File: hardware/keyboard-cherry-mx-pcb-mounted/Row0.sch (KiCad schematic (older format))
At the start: 28 parts, among them SW1 ESC, SW10 F12, SW11 F5, SW12 Delete, SW13 F6, SW14 F7, SW2 F8, SW3 F1, SW4 F9, SW5 F2, SW6 F10, SW7 F2, SW8 F11, SW9 F4

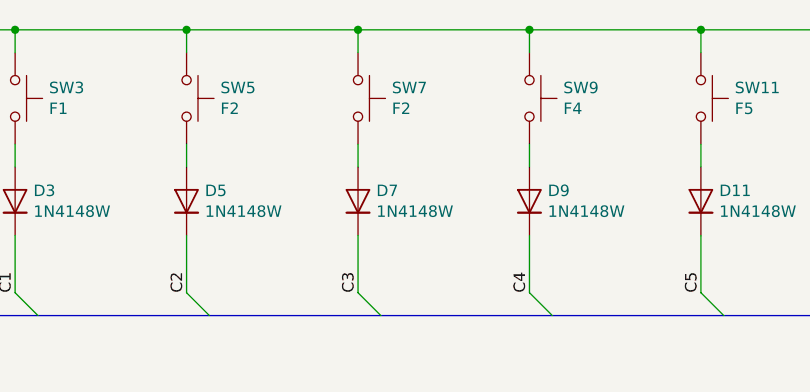
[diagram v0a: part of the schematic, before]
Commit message: Adds general layout for the custom keyboard.
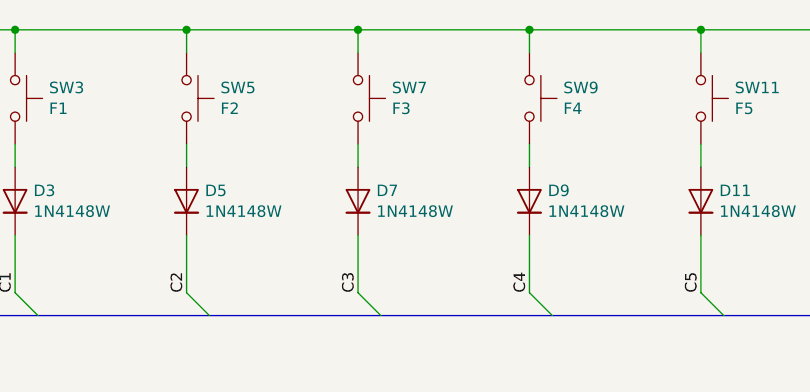
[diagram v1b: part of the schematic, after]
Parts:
- SW7: value F2 -> F3
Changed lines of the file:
@@
 AR Path="/5E697948/5E6CDE4B/5E6D9975" Ref="SW7"  Part="1"
 F 0 "SW7" V 5304 2848 50  0000 L CNN
-F 1 "F2" V 5395 2848 50  0000 L CNN
+F 1 "F3" V 5395 2848 50  0000 L CNN
 F 2 "Button_Switch_Keyboard:SW_Cherry_MX_1.00u_PCB" H 5350 2900 50  0001 C CNN
 F 3 "~" H 5350 2900 50  0001 C CNN
@@
 Text Label 2800 3650 2    50   ~ 0
 C[0..15]
+Connection ~ 6850 4500
+Wire Wire Line
+	6850 4500 9350 4500
+Wire Wire Line
+	9350 2400 9350 4500
+Connection ~ 8350 2400
+Wire Wire Line
+	8350 2400 9350 2400
 Wire Bus Line
 	2800 5750 6950 5750
 Wire Bus Line
 	2800 3650 8450 3650
-Connection ~ 6850 4500
-Wire Wire Line
-	6850 4500 9350 4500
-Wire Wire Line
-	9350 2400 9350 4500
-Connection ~ 8350 2400
-Wire Wire Line
-	8350 2400 9350 2400
 $EndSCHEMATC

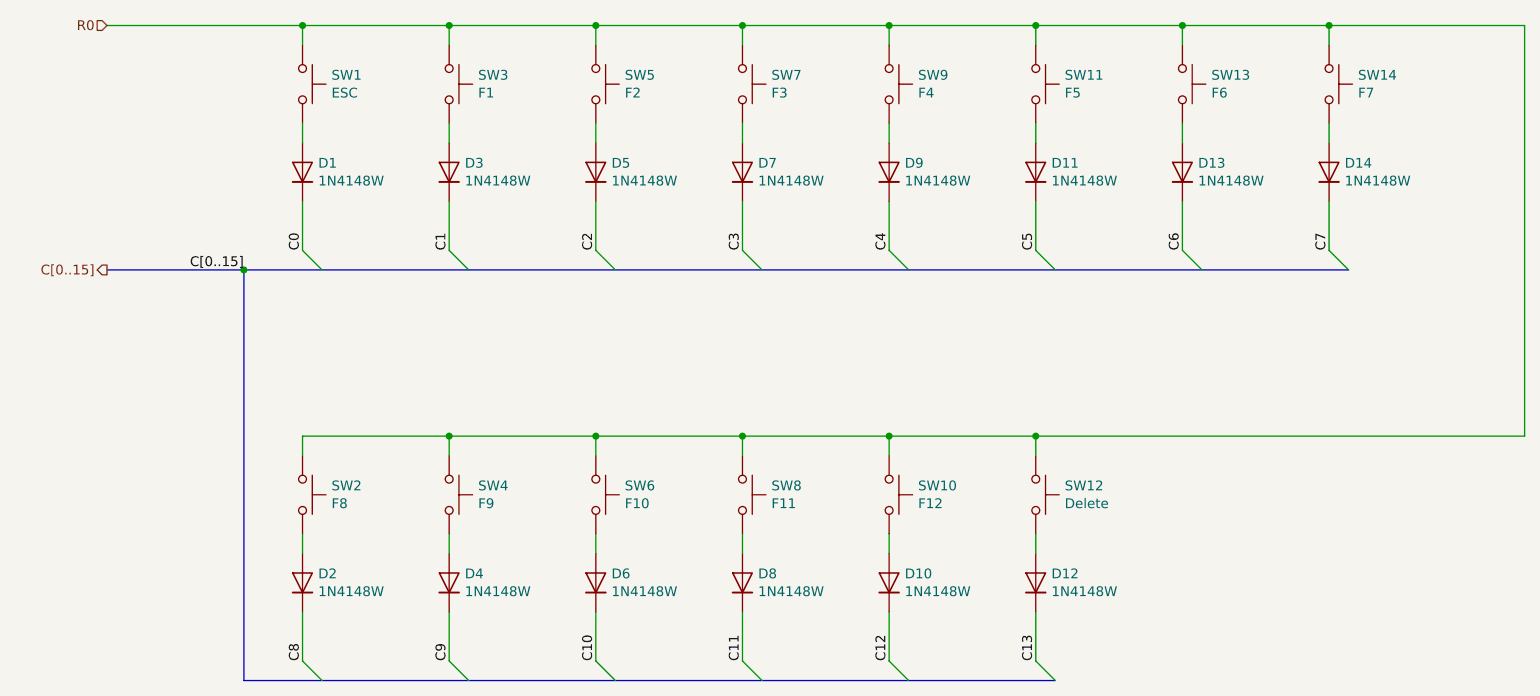
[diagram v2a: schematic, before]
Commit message: Adds completed sensor and power connections. Still need to add USB footprint then sch are done for version 1.0
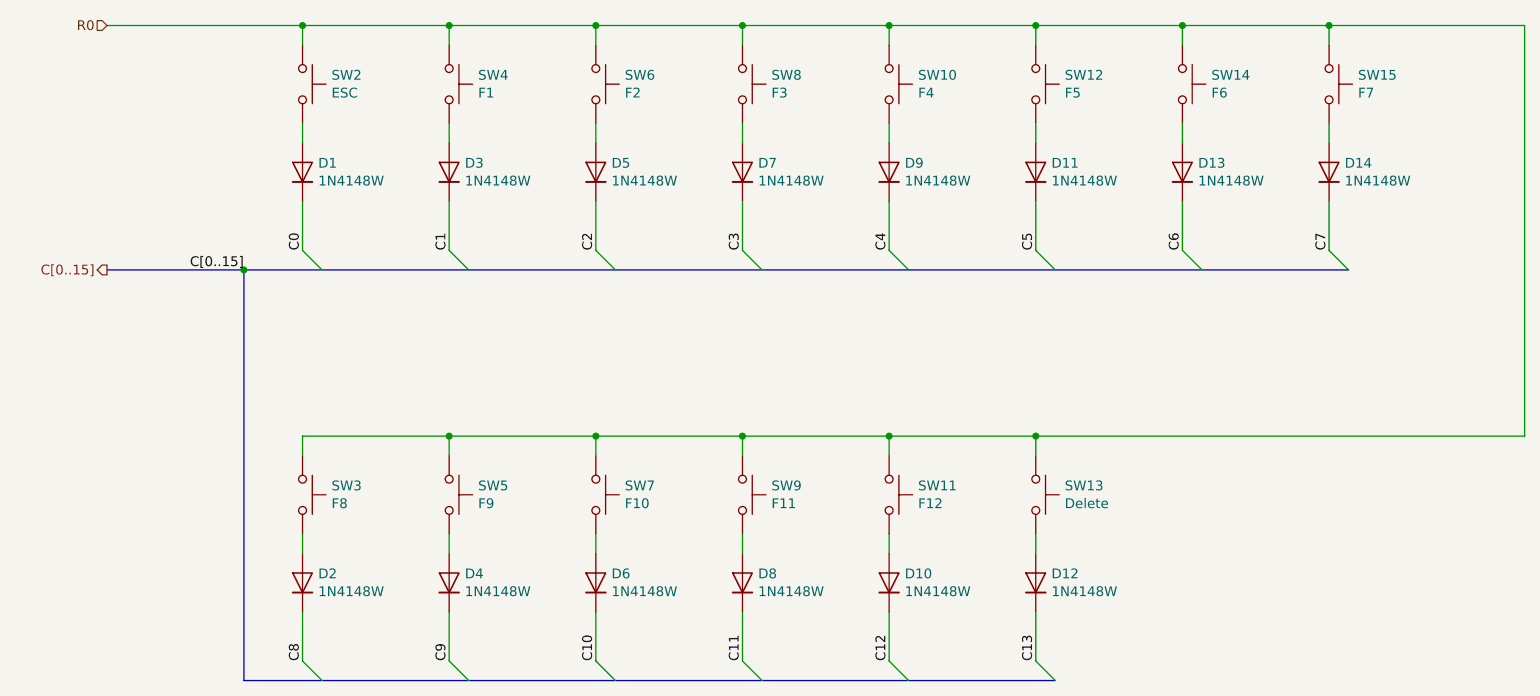
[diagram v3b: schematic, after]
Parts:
- renumbered SW9 to SW10, SW10 to SW11, SW11 to SW12, SW12 to SW13, SW13 to SW14, SW14 to SW15, SW1 to SW2, SW2 to SW3, SW3 to SW4, SW4 to SW5, SW5 to SW6, SW6 to SW7, SW7 to SW8, SW8 to SW9
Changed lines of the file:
@@
 P 3100 2700
 AR Path="/5E697948/5E6D9949" Ref="SW?"  Part="1"
-AR Path="/5E697948/5E6CDE4B/5E6D9949" Ref="SW1"  Part="1"
-F 0 "SW1" V 3054 2848 50  0000 L CNN
+AR Path="/5E697948/5E6CDE4B/5E6D9949" Ref="SW2"  Part="1"
+F 0 "SW2" V 3054 2848 50  0000 L CNN
 F 1 "ESC" V 3145 2848 50  0000 L CNN
 F 2 "Button_Switch_Keyboard:SW_Cherry_MX_1.00u_PCB" H 3100 2900 50  0001 C CNN
@@
 P 3850 2700
 AR Path="/5E697948/5E6D9959" Ref="SW?"  Part="1"
-AR Path="/5E697948/5E6CDE4B/5E6D9959" Ref="SW3"  Part="1"
-F 0 "SW3" V 3804 2848 50  0000 L CNN
+AR Path="/5E697948/5E6CDE4B/5E6D9959" Ref="SW4"  Part="1"
+F 0 "SW4" V 3804 2848 50  0000 L CNN
 F 1 "F1" V 3895 2848 50  0000 L CNN
 F 2 "Button_Switch_Keyboard:SW_Cherry_MX_1.00u_PCB" H 3850 2900 50  0001 C CNN
@@
 P 4600 2700
 AR Path="/5E697948/5E6D9967" Ref="SW?"  Part="1"
-AR Path="/5E697948/5E6CDE4B/5E6D9967" Ref="SW5"  Part="1"
-F 0 "SW5" V 4554 2848 50  0000 L CNN
+AR Path="/5E697948/5E6CDE4B/5E6D9967" Ref="SW6"  Part="1"
+F 0 "SW6" V 4554 2848 50  0000 L CNN
 F 1 "F2" V 4645 2848 50  0000 L CNN
 F 2 "Button_Switch_Keyboard:SW_Cherry_MX_1.00u_PCB" H 4600 2900 50  0001 C CNN
@@
 P 5350 2700
 AR Path="/5E697948/5E6D9975" Ref="SW?"  Part="1"
-AR Path="/5E697948/5E6CDE4B/5E6D9975" Ref="SW7"  Part="1"
-F 0 "SW7" V 5304 2848 50  0000 L CNN
+AR Path="/5E697948/5E6CDE4B/5E6D9975" Ref="SW8"  Part="1"
+F 0 "SW8" V 5304 2848 50  0000 L CNN
 F 1 "F3" V 5395 2848 50  0000 L CNN
 F 2 "Button_Switch_Keyboard:SW_Cherry_MX_1.00u_PCB" H 5350 2900 50  0001 C CNN
@@
 P 6100 2700
 AR Path="/5E697948/5E6D9983" Ref="SW?"  Part="1"
-AR Path="/5E697948/5E6CDE4B/5E6D9983" Ref="SW9"  Part="1"
-F 0 "SW9" V 6054 2848 50  0000 L CNN
+AR Path="/5E697948/5E6CDE4B/5E6D9983" Ref="SW10"  Part="1"
+F 0 "SW10" V 6054 2848 50  0000 L CNN
 F 1 "F4" V 6145 2848 50  0000 L CNN
 F 2 "Button_Switch_Keyboard:SW_Cherry_MX_1.00u_PCB" H 6100 2900 50  0001 C CNN
@@
 P 6850 2700
 AR Path="/5E697948/5E6D9991" Ref="SW?"  Part="1"
-AR Path="/5E697948/5E6CDE4B/5E6D9991" Ref="SW11"  Part="1"
-F 0 "SW11" V 6804 2848 50  0000 L CNN
+AR Path="/5E697948/5E6CDE4B/5E6D9991" Ref="SW12"  Part="1"
+F 0 "SW12" V 6804 2848 50  0000 L CNN
 F 1 "F5" V 6895 2848 50  0000 L CNN
 F 2 "Button_Switch_Keyboard:SW_Cherry_MX_1.00u_PCB" H 6850 2900 50  0001 C CNN
@@
 P 7600 2700
 AR Path="/5E697948/5E6D999F" Ref="SW?"  Part="1"
-AR Path="/5E697948/5E6CDE4B/5E6D999F" Ref="SW13"  Part="1"
-F 0 "SW13" V 7554 2848 50  0000 L CNN
+AR Path="/5E697948/5E6CDE4B/5E6D999F" Ref="SW14"  Part="1"
+F 0 "SW14" V 7554 2848 50  0000 L CNN
 F 1 "F6" V 7645 2848 50  0000 L CNN
 F 2 "Button_Switch_Keyboard:SW_Cherry_MX_1.00u_PCB" H 7600 2900 50  0001 C CNN
@@
 P 8350 2700
 AR Path="/5E697948/5E6D99AD" Ref="SW?"  Part="1"
-AR Path="/5E697948/5E6CDE4B/5E6D99AD" Ref="SW14"  Part="1"
-F 0 "SW14" V 8304 2848 50  0000 L CNN
+AR Path="/5E697948/5E6CDE4B/5E6D99AD" Ref="SW15"  Part="1"
+F 0 "SW15" V 8304 2848 50  0000 L CNN
 F 1 "F7" V 8395 2848 50  0000 L CNN
 F 2 "Button_Switch_Keyboard:SW_Cherry_MX_1.00u_PCB" H 8350 2900 50  0001 C CNN
@@
 P 3100 4800
 AR Path="/5E697948/5E6D99BB" Ref="SW?"  Part="1"
-AR Path="/5E697948/5E6CDE4B/5E6D99BB" Ref="SW2"  Part="1"
-F 0 "SW2" V 3054 4948 50  0000 L CNN
+AR Path="/5E697948/5E6CDE4B/5E6D99BB" Ref="SW3"  Part="1"
+F 0 "SW3" V 3054 4948 50  0000 L CNN
 F 1 "F8" V 3145 4948 50  0000 L CNN
 F 2 "Button_Switch_Keyboard:SW_Cherry_MX_1.00u_PCB" H 3100 5000 50  0001 C CNN
@@
 P 3850 4800
 AR Path="/5E697948/5E6D99C9" Ref="SW?"  Part="1"
-AR Path="/5E697948/5E6CDE4B/5E6D99C9" Ref="SW4"  Part="1"
-F 0 "SW4" V 3804 4948 50  0000 L CNN
+AR Path="/5E697948/5E6CDE4B/5E6D99C9" Ref="SW5"  Part="1"
+F 0 "SW5" V 3804 4948 50  0000 L CNN
 F 1 "F9" V 3895 4948 50  0000 L CNN
 F 2 "Button_Switch_Keyboard:SW_Cherry_MX_1.00u_PCB" H 3850 5000 50  0001 C CNN
@@
 P 4600 4800
 AR Path="/5E697948/5E6D99D7" Ref="SW?"  Part="1"
-AR Path="/5E697948/5E6CDE4B/5E6D99D7" Ref="SW6"  Part="1"
-F 0 "SW6" V 4554 4948 50  0000 L CNN
+AR Path="/5E697948/5E6CDE4B/5E6D99D7" Ref="SW7"  Part="1"
+F 0 "SW7" V 4554 4948 50  0000 L CNN
 F 1 "F10" V 4645 4948 50  0000 L CNN
 F 2 "Button_Switch_Keyboard:SW_Cherry_MX_1.00u_PCB" H 4600 5000 50  0001 C CNN
@@
 P 5350 4800
 AR Path="/5E697948/5E6D99E5" Ref="SW?"  Part="1"
-AR Path="/5E697948/5E6CDE4B/5E6D99E5" Ref="SW8"  Part="1"
-F 0 "SW8" V 5304 4948 50  0000 L CNN
+AR Path="/5E697948/5E6CDE4B/5E6D99E5" Ref="SW9"  Part="1"
+F 0 "SW9" V 5304 4948 50  0000 L CNN
 F 1 "F11" V 5395 4948 50  0000 L CNN
 F 2 "Button_Switch_Keyboard:SW_Cherry_MX_1.00u_PCB" H 5350 5000 50  0001 C CNN
@@
 P 6100 4800
 AR Path="/5E697948/5E6D99F3" Ref="SW?"  Part="1"
-AR Path="/5E697948/5E6CDE4B/5E6D99F3" Ref="SW10"  Part="1"
-F 0 "SW10" V 6054 4948 50  0000 L CNN
+AR Path="/5E697948/5E6CDE4B/5E6D99F3" Ref="SW11"  Part="1"
+F 0 "SW11" V 6054 4948 50  0000 L CNN
 F 1 "F12" V 6145 4948 50  0000 L CNN
 F 2 "Button_Switch_Keyboard:SW_Cherry_MX_1.00u_PCB" H 6100 5000 50  0001 C CNN
@@
 P 6850 4800
 AR Path="/5E697948/5E6D9A01" Ref="SW?"  Part="1"
-AR Path="/5E697948/5E6CDE4B/5E6D9A01" Ref="SW12"  Part="1"
-F 0 "SW12" V 6804 4948 50  0000 L CNN
+AR Path="/5E697948/5E6CDE4B/5E6D9A01" Ref="SW13"  Part="1"
+F 0 "SW13" V 6804 4948 50  0000 L CNN
 F 1 "Delete" V 6895 4948 50  0000 L CNN
 F 2 "Button_Switch_Keyboard:SW_Cherry_MX_1.00u_PCB" H 6850 5000 50  0001 C CNN
